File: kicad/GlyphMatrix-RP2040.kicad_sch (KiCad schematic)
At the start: 36 parts, among them J1 Conn_01x04, SW1 SW_Push, SW2 SW_Push, U1 W25Q128JVS, U2 USBLC6-2SC6, U3 XC6206PxxxMR-Regulator_Linear, Y1 12MHz

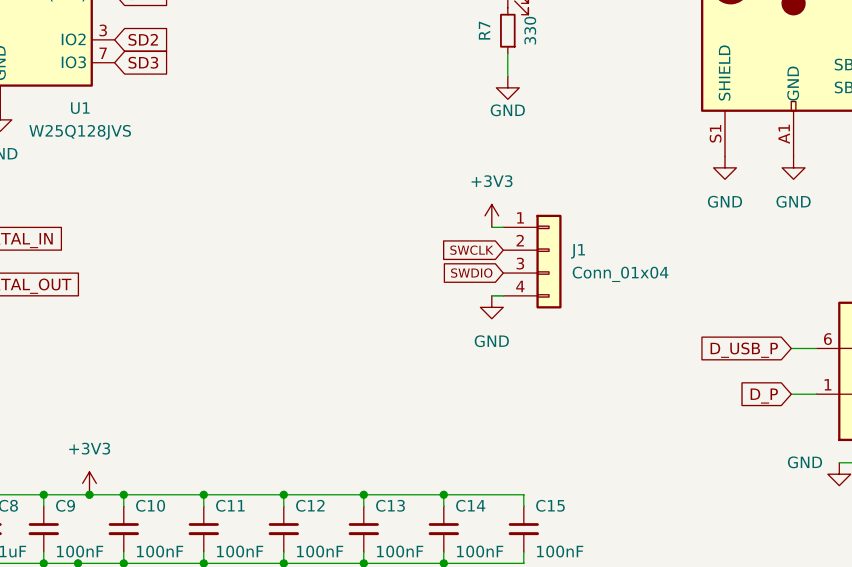
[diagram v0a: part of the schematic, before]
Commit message: updated schematic for GlyphMatrix (#20)
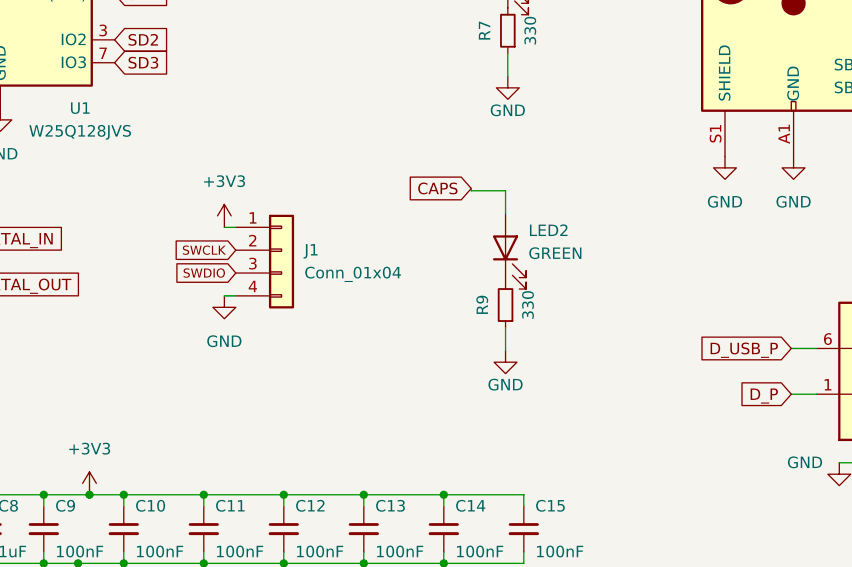
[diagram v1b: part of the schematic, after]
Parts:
- added LED2: GREEN, LED_SMD:LED_0603_1608Metric_Pad1.05x0.95mm_HandSolder, symbol Device:LED
- added R9: 330, Resistor_SMD:R_0603_1608Metric, symbol Device:R_Small
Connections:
- net CAPS: now also LED2.2 (A)
- net GND: now also R9.1
- new net: LED2.1 (K), R9.2
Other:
- moved on the sheet: J1
